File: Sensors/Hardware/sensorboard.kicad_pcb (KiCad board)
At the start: 4 copper layers, 100 x 50 mm, 296 parts, among them J1 RBUS, J10 1053131104, J11 1053131104, J12 1053131104, J13 1053131104, J14 1053131104, J15 USB_C_Receptacle_USB2.0, J16 Micro_SD_Card_Det, J2 Conn_Coaxial, J3 1053131104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

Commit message: update (tps and filters)
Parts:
- added C13: 10uF, Capacitor_SMD:C_0603_1608Metric, F.Cu at (137.9, 149.5)
- added C14: 2.2uF, Capacitor_SMD:C_0603_1608Metric, F.Cu at (140.9, 155.2)
- added R64: 2.184M, Resistor_SMD:R_0603_1608Metric, F.Cu at (132.0, 151.3)
- added R67: 390k, Resistor_SMD:R_0603_1608Metric, F.Cu at (132.0, 154.7)
- added R68: 200k, Resistor_SMD:R_0603_1608Metric, F.Cu at (134.7, 158.2)
- added R72: 1M, Resistor_SMD:R_0603_1608Metric, F.Cu at (138.4, 158.2)
- added R73: 1.8M, Resistor_SMD:R_0603_1608Metric, F.Cu at (136.9, 158.2)
- C53: footprint Capacitor_SMD:C_0603_1608Metric -> iclr:CAPC2012X145N
- R69, R70, R71: footprint Resistor_SMD:R_0402_1005Metric -> Resistor_SMD:R_0603_1608Metric
- moved C51 164.1 mm to (154.4, 156.2)
- moved R58 164.1 mm to (149.7, 156.1)
- moved R59 164.1 mm to (145.9, 151.5)
- moved R60 163.8 mm to (158.7, 156.0)
- moved C52 163.8 mm to (153.3, 159.1)
- moved R61 163.8 mm to (162.5, 154.4)
- moved R62 163.8 mm to (161.6, 150.9)
- moved L4 161.0 mm to (141.4, 151.7), turned to -90 degrees
- moved TC1 159.3 mm to (254.0, 93.9)
- moved U2 159.3 mm to (247.1, 92.9)
- moved C15 159.3 mm to (247.1, 99.1)
- moved C16 159.3 mm to (250.0, 97.2)
- moved C17 159.3 mm to (250.0, 99.1)
- moved C18 159.3 mm to (247.1, 97.2)
- moved R8 159.3 mm to (244.2, 97.2)
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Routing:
- net +5V: track 2.03 -> 13.7 mm, vias 1 -> 2
- net Net-(R61-Pad1): track 0.00 -> 11.2 mm
- net +3V3: track 3.65 -> 13.1 mm, vias 2 -> 5
- net Net-(R60-Pad1): track 0.00 -> 5.38 mm
- net Net-(J7-Pad1): track 5.10 -> 0.00 mm
- net Net-(R58-Pad2): track 0.00 -> 4.50 mm
- net Net-(JP13-Pad1): track 3.63 -> 0.02 mm
- net Net-(L4-Pad2): track 0.00 -> 3.32 mm
- net Net-(J7-Pad3): track 3.29 -> 0.07 mm
- net Net-(JP13-Pad3): track 3.57 -> 0.37 mm
- net /Power/BBIN: track 3.68 -> 6.36 mm
- net GND: track 6.73 -> 8.63 mm, vias 8 -> 21
- net RBUS_uC_V: track 0.00 -> 1.83 mm
- net Net-(J7-Pad2): track 2.69 -> 1.10 mm

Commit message: redimensioning to 120x50mm
also finished tps
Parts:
- removed the C13 at (137.9, 149.5)
- removed the C14 at (140.9, 155.2)
- removed the R64 at (132.0, 151.3)
- removed the R67 at (132.0, 154.7)
- removed the R68 at (134.7, 158.2)
- removed the R72 at (138.4, 158.2)
- removed the R73 at (136.9, 158.2)
- C51, C52: footprint Capacitor_SMD:C_0402_1005Metric -> Capacitor_SMD:C_0603_1608Metric
- R59, R60: footprint Resistor_SMD:R_0402_1005Metric -> Resistor_SMD:R_0603_1608Metric
- moved TC1 174.9 mm to (98.3, 14.3)
- moved C15 166.8 mm to (100.1, 20.4)
- moved C16 166.8 mm to (102.9, 18.4)
- moved C17 166.8 mm to (102.9, 20.4)
- moved C18 166.8 mm to (100.1, 18.4)
- moved R8 166.8 mm to (97.2, 18.4)
- moved R9 166.8 mm to (97.2, 20.4)
- moved U2 161.7 mm to (100.6, 24.6)
- moved C23 157.6 mm to (90.0, 19.3)
- moved C24 157.6 mm to (92.9, 17.4)
- moved C25 157.6 mm to (92.9, 19.3)
- moved C26 157.6 mm to (90.0, 17.4)
- moved R12 157.6 mm to (87.1, 17.4)
- moved R13 157.6 mm to (87.1, 19.4)
- moved TC3 156.3 mm to (90.0, 31.0)
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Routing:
- net +3V3: track 13.1 -> 12.1 mm
- net GND: vias 21 -> 24
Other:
- board size 100 x 50 mm -> 120 x 50 mm

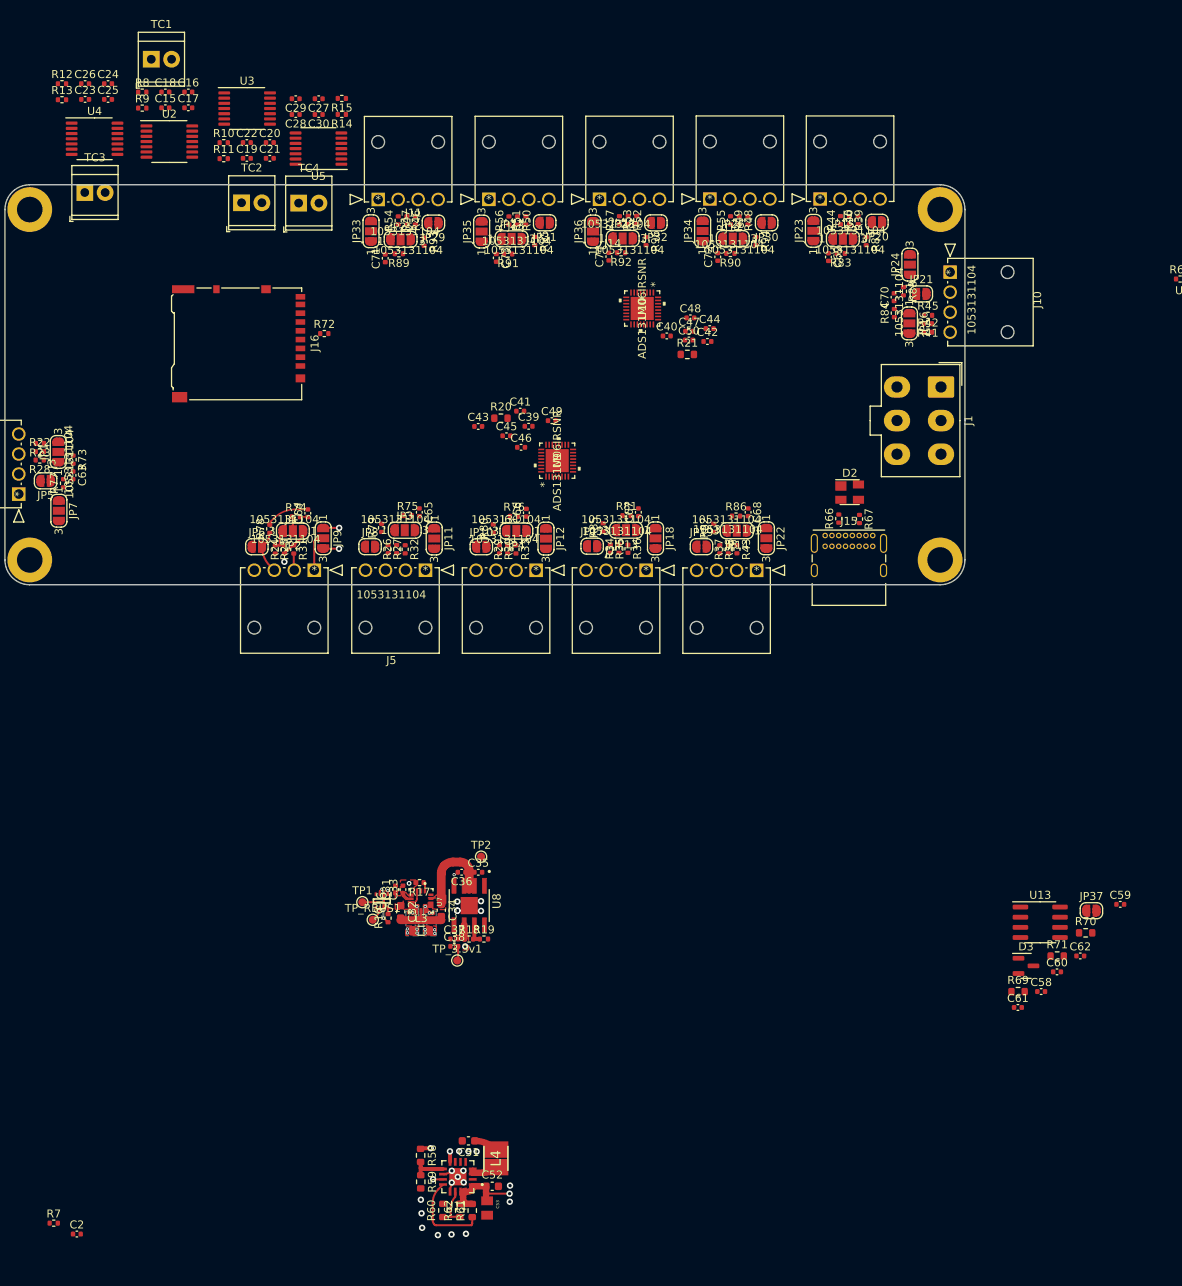
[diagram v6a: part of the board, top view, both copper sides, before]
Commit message: update and thermocouple template layout
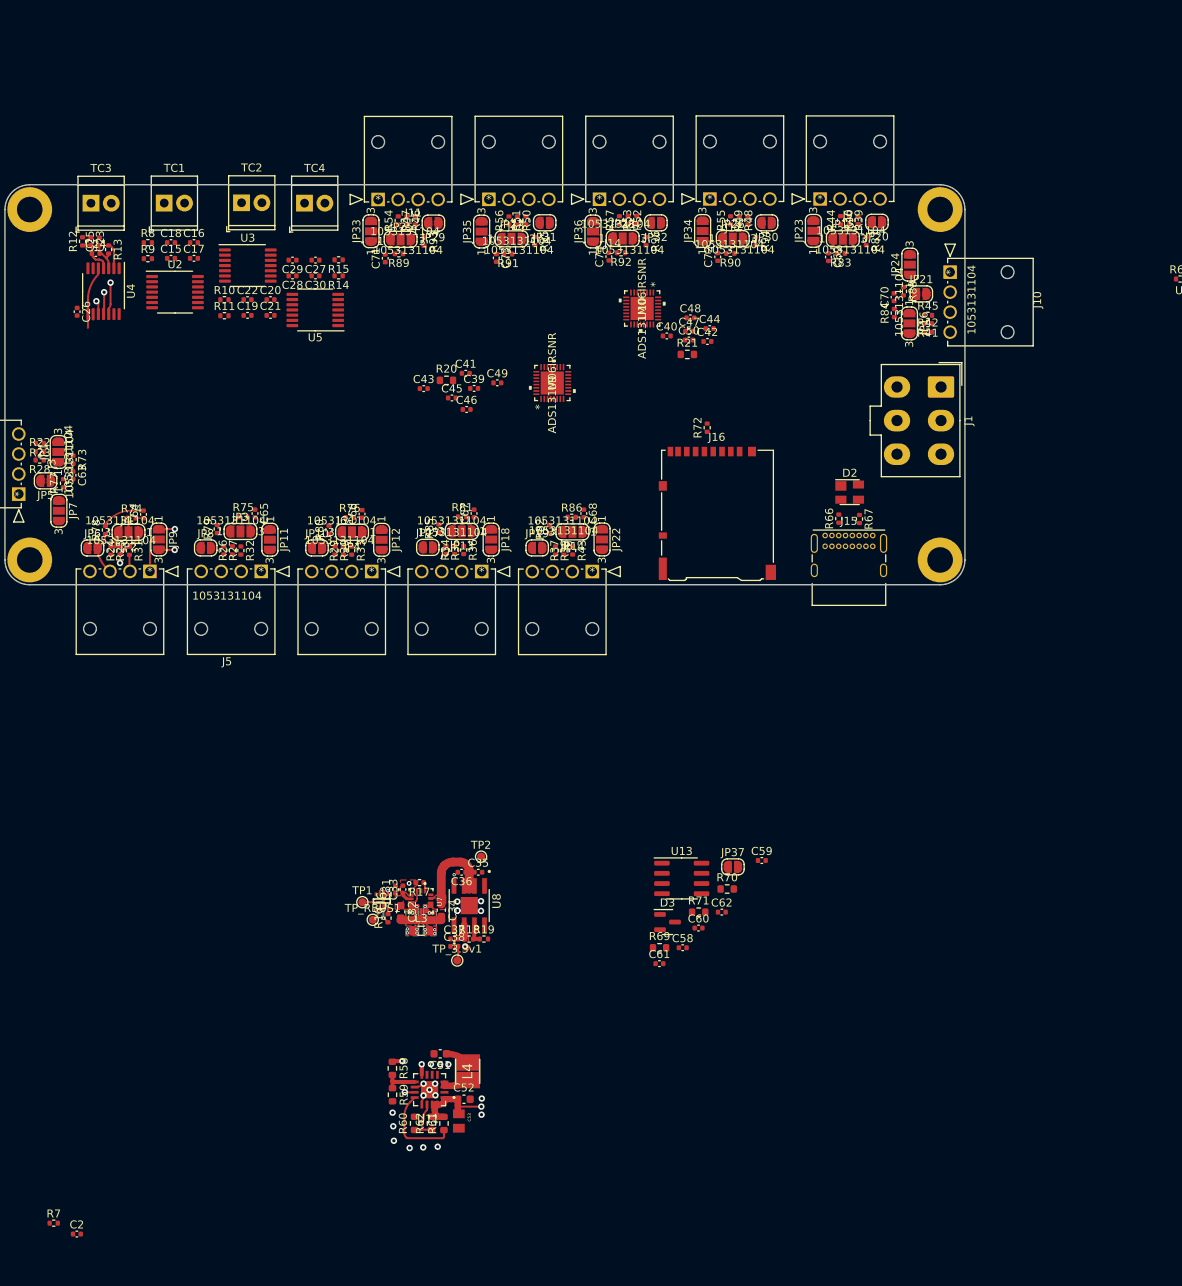
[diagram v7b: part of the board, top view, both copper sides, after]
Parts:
- moved J16 63.5 mm to (169.1, 71.1), turned to 0 degrees
- moved R72 49.3 mm to (167.8, 60.4), turned to 90 degrees
- moved C58 45.1 mm to (164.7, 125.4)
- moved C60 45.1 mm to (166.7, 122.9)
- moved C61 45.1 mm to (161.8, 127.4)
- moved D3 45.1 mm to (162.8, 122.2)
- moved JP37 45.1 mm to (171.0, 115.3)
- moved R70 45.1 mm to (170.3, 118.0)
- moved R71 45.1 mm to (166.7, 120.9)
- moved U13 45.1 mm to (164.6, 116.7)
- moved C59 45.1 mm to (174.6, 114.5)
- moved C62 45.1 mm to (169.6, 120.9)
- moved R69 45.1 mm to (161.8, 125.4)
- moved C26 28.5 mm to (89.0, 45.9), turned to -90 degrees
- moved C24 21.3 mm to (91.4, 38.6)
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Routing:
- net +3V3: track 12.1 -> 19.2 mm
- net Net-(C23-Pad2): track 0.00 -> 4.91 mm
- net Net-(C24-Pad2): track 0.00 -> 4.11 mm
- net /MOSI: track 0.00 -> 3.99 mm, vias 0 -> 1
- net Net-(R13-Pad1): track 0.00 -> 2.85 mm
- net /MISO: track 0.00 -> 2.75 mm, vias 0 -> 1
- net /SCLK: track 0.00 -> 1.85 mm, vias 0 -> 1
- net /CS3: track 0.00 -> 0.69 mm

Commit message: update
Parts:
- added C31: 160pF, Capacitor_SMD:C_0603_1608Metric, F.Cu at (158.7, 118.8)
- added C71: 100nF, Capacitor_SMD:C_0603_1608Metric, F.Cu at (157.1, 121.7)
- added C72: 10uF, Capacitor_SMD:C_0603_1608Metric, F.Cu at (158.7, 121.8)
- added C73: 0.1uF, Capacitor_SMD:C_0603_1608Metric, F.Cu at (171.2, 123.3)
- added C74: 220pF, Capacitor_SMD:C_0603_1608Metric, F.Cu at (168.6, 119.0)
- added C75: 220 pF, Capacitor_SMD:C_0603_1608Metric, F.Cu at (168.6, 124.4)
- moved ENJUMPER1 144.1 mm to (82.5, 40.0)
- moved C2 121.2 mm to (85.5, 40.0)
- moved C12 102.8 mm to (85.6, 49.7)
- moved BOOTJUMPER1 99.4 mm to (82.6, 49.5)
- moved R7 29.8 mm to (61.9, 142.5)
- moved C59 19.0 mm to (157.1, 121.8), turned to 90 degrees
- moved C21 11.4 mm to (106.6, 37.0), turned to 90 degrees
- moved R14 11.2 mm to (111.4, 37.1), turned to 90 degrees
- moved C61 10.7 mm to (168.5, 119.0), turned to 180 degrees
- moved C19 10.4 mm to (105.6, 37.0), turned to -90 degrees
- moved C30 10.1 mm to (109.5, 45.4), turned to -90 degrees
- moved D3 10.0 mm to (172.4, 119.2), turned to -90 degrees
- moved C18 9.84 mm to (95.8, 45.7), turned to -90 degrees
- moved U9 9.83 mm to (145.0, 64.0)
- moved C20 9.23 mm to (106.1, 38.5)
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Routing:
- net +3V3: track 19.2 -> 110.8 mm, vias 5 -> 7
- net +5V: track 13.7 -> 84.8 mm, vias 2 -> 4
- net /MOSI: track 3.99 -> 37.9 mm, vias 1 -> 4
- net /MISO: track 2.75 -> 33.9 mm, vias 1 -> 4
- net /SCLK: track 1.85 -> 30.6 mm, vias 1 -> 4
- net /CAN-: track 0.00 -> 17.2 mm
- net /CAN-BUS/Vref: track 0.00 -> 14.7 mm, vias 0 -> 2
- net Net-(J3-Pad3): track 0.00 -> 11.7 mm
- net /CAN+: track 0.00 -> 9.72 mm
- net Net-(C60-Pad1): track 0.00 -> 6.45 mm
- net Net-(J3-Pad1): track 0.00 -> 5.54 mm
- net Net-(JP1-Pad1): track 0.00 -> 3.34 mm
- net Net-(JP1-Pad3): track 0.00 -> 2.89 mm
- net Net-(J3-Pad2): track 0.00 -> 2.79 mm
- net /CAN_TX: track 0.00 -> 2.74 mm
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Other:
- board text added: "TX_LED1"
